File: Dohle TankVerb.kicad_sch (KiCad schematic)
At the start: 10 parts, among them J1 AudioJack3, J2 AudioJack3, J3 PWR, J4 Conn_01x07_Female, SW1 3pdt_footswitch, SW2 SW_Push

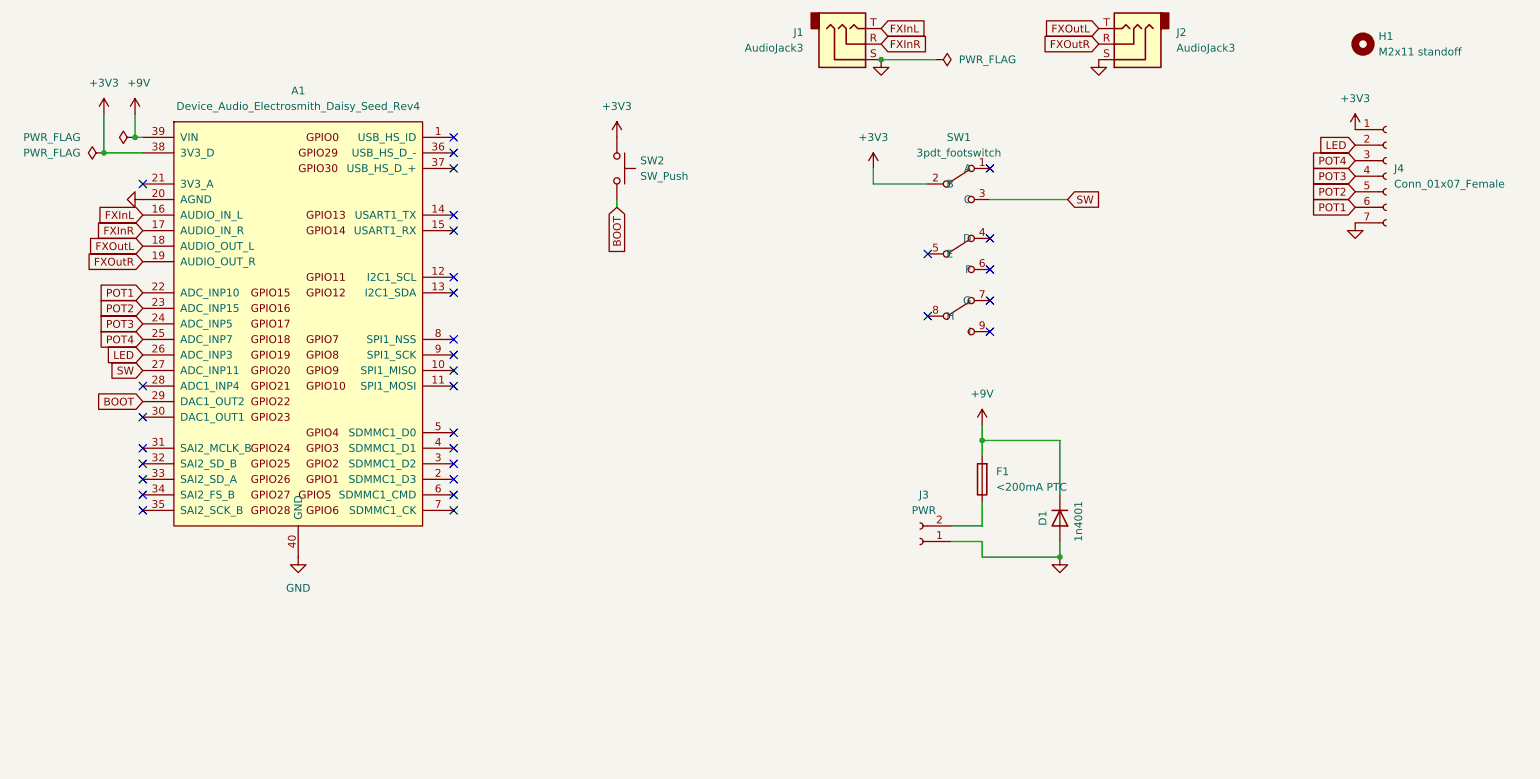
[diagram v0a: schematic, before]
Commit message: Finish adding the expression pedal. New release.
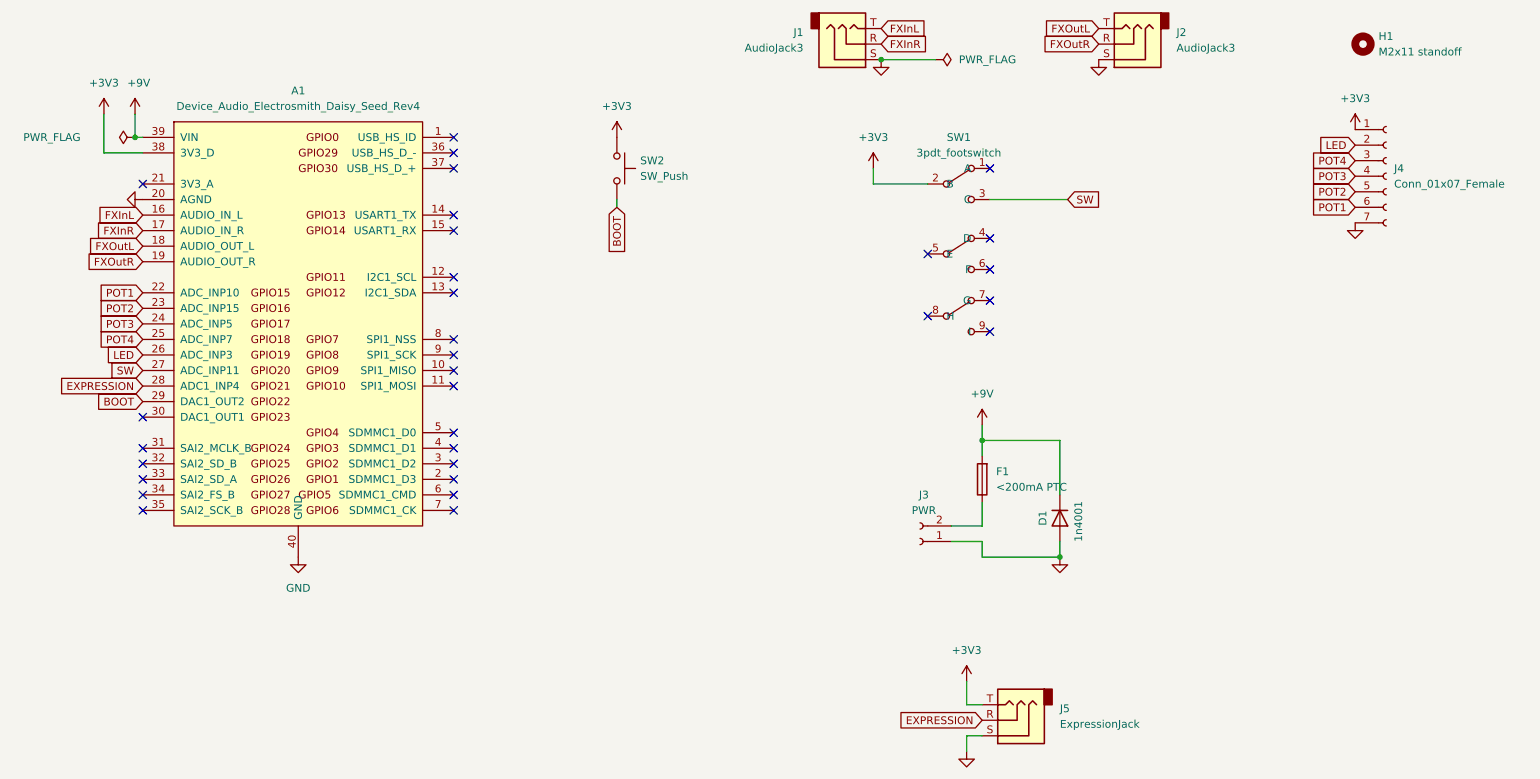
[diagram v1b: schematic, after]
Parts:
- added J5: ExpressionJack, BirdFootprints:ExpressionJack, symbol Connector:AudioJack3
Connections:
- net +3V3: now also J5.T
- net GND: now also J5.S
- net EXPRESSION: now reaches A1.28 (ADC1_INP4)
- net EXPRESSION: now also J5.R
- no-connect marks 32 -> 31
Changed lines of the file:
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@@
   (junction (at 39.37 48.26) (diameter 0) (color 0 0 0 0)
-  )
-  (junction (at 34.29 50.8) (diameter 0) (color 0 0 0 0)
   )
   (junction (at 190.5 116.84) (diameter 0) (color 0 0 0 0)
@@
   (no_connect (at 40.64 106.68))
   (no_connect (at 40.64 109.22))
-  (no_connect (at 40.64 88.9))
   (no_connect (at 91.44 109.22))
   (no_connect (at 91.44 106.68))
@@
     (stroke (width 0) (type default) (color 0 0 0 0))
   )
+  (wire (pts (xy 177.8 146.05) (xy 175.26 146.05))
+    (stroke (width 0) (type default) (color 0 0 0 0))
+  )
   (wire (pts (xy 40.64 50.8) (xy 34.29 50.8))
     (stroke (width 0) (type default) (color 0 0 0 0))
   )
+  (wire (pts (xy 175.26 140.97) (xy 177.8 140.97))
+    (stroke (width 0) (type default) (color 0 0 0 0))
+  )
+  (wire (pts (xy 175.26 146.05) (xy 175.26 148.59))
+    (stroke (width 0) (type default) (color 0 0 0 0))
+  )
   (wire (pts (xy 161.29 35.56) (xy 170.18 35.56))
     (stroke (width 0) (type default) (color 0 0 0 0))
   )
   (wire (pts (xy 177.8 111.76) (xy 177.8 107.95))
+    (stroke (width 0) (type default) (color 0 0 0 0))
+  )
+  (wire (pts (xy 175.26 137.16) (xy 175.26 140.97))
     (stroke (width 0) (type default) (color 0 0 0 0))
   )
@@
     )
   )
+  (global_label "EXPRESSION" (shape input) (at 177.8 143.51 180) (fields_autoplaced)
+    (effects (font (size 1.27 1.27)) (justify right))
+    (property "Intersheet References" "${INTERSHEET_REFS}" (id 0) (at 163.6545 143.4306 0)
+      (effects (font (size 1.27 1.27)) (justify right) hide)
+    )
+  )
   (global_label "FXInR" (shape input) (at 161.29 33.02 0) (fields_autoplaced)
     (effects (font (size 1.27 1.27)) (justify left))
@@
     (effects (font (size 1.27 1.27)) (justify right))
     (property "Intersheet References" "${INTERSHEET_REFS}" (id 0) (at 231.5693 57.2294 0)
+      (effects (font (size 1.27 1.27)) (justify right) hide)
+    )
+  )
+  (global_label "EXPRESSION" (shape input) (at 40.64 88.9 180) (fields_autoplaced)
+    (effects (font (size 1.27 1.27)) (justify right))
+    (property "Intersheet References" "${INTERSHEET_REFS}" (id 0) (at 26.4945 88.8206 0)
       (effects (font (size 1.27 1.27)) (justify right) hide)
     )
@@
     (pin "9")
   )
+  (symbol (lib_id "power:GND") (at 175.26 148.59 0) (unit 1)
+    (in_bom yes) (on_board yes) (fields_autoplaced)
+    (property "Reference" "#PWR02" (id 0) (at 175.26 154.94 0)
+      (effects (font (size 1.27 1.27)) hide)
+    )
+    (property "Value" "GND" (id 1) (at 175.26 153.035 0)
+      (effects (font (size 1.27 1.27)) hide)
+    )
+    (property "Footprint" "" (id 2) (at 175.26 148.59 0)
+      (effects (font (size 1.27 1.27)) hide)
+    )
+    (property "Datasheet" "" (id 3) (at 175.26 148.59 0)
+      (effects (font (size 1.27 1.27)) hide)
+    )
+    (pin "1")
+  )
   (symbol (lib_id "power:PWR_FLAG") (at 39.37 48.26 90) (unit 1)
     (in_bom yes) (on_board yes)
@@
     (pin "T")
   )
+  (symbol (lib_id "Connector:AudioJack3") (at 182.88 143.51 180) (unit 1)
+    (in_bom yes) (on_board yes) (fields_autoplaced)
+    (property "Reference" "J5" (id 0) (at 190.5 141.6049 0)
+      (effects (font (size 1.27 1.27)) (justify right))
+    )
+    (property "Value" "ExpressionJack" (id 1) (at 190.5 144.1449 0)
+      (effects (font (size 1.27 1.27)) (justify right))
+    )
+    (property "Footprint" "BirdFootprints:ExpressionJack" (id 2) (at 182.88 143.51 0)
+      (effects (font (size 1.27 1.27)) hide)
+    )
+    (property "Datasheet" "~" (id 3) (at 182.88 143.51 0)
+      (effects (font (size 1.27 1.27)) hide)
+    )
+    (pin "R")
+    (pin "S")
+    (pin "T")
+  )
   (symbol (lib_id "power:GND") (at 238.76 62.23 0) (unit 1)
     (in_bom yes) (on_board yes) (fields_autoplaced)
@@
     )
     (property "Datasheet" "" (id 3) (at 34.29 44.45 0)
-      (effects (font (size 1.27 1.27)) hide)
-    )
-    (pin "1")
-  )
-  (symbol (lib_id "power:PWR_FLAG") (at 34.29 50.8 90) (unit 1)
-    (in_bom yes) (on_board yes) (fields_autoplaced)
-    (property "Reference" "#FLG0101" (id 0) (at 32.385 50.8 0)
-      (effects (font (size 1.27 1.27)) hide)
-    )
-    (property "Value" "PWR_FLAG" (id 1) (at 30.48 50.7999 90)
-      (effects (font (size 1.27 1.27)) (justify left))
-    )
-    (property "Footprint" "" (id 2) (at 34.29 50.8 0)
-      (effects (font (size 1.27 1.27)) hide)
-    )
-    (property "Datasheet" "~" (id 3) (at 34.29 50.8 0)
       (effects (font (size 1.27 1.27)) hide)
     )
@@
     (pin "9")
   )
+  (symbol (lib_id "power:+3V3") (at 175.26 137.16 0) (unit 1)
+    (in_bom yes) (on_board yes) (fields_autoplaced)
+    (property "Reference" "#PWR01" (id 0) (at 175.26 140.97 0)
+      (effects (font (size 1.27 1.27)) hide)
+    )
+    (property "Value" "+3V3" (id 1) (at 175.26 132.08 0))
+    (property "Footprint" "" (id 2) (at 175.26 137.16 0)
+      (effects (font (size 1.27 1.27)) hide)
+    )
+    (property "Datasheet" "" (id 3) (at 175.26 137.16 0)
+      (effects (font (size 1.27 1.27)) hide)
+    )
+    (pin "1")
+  )
   (symbol (lib_id "Connector:Conn_01x02_Female") (at 167.64 114.3 180) (unit 1)
     (in_bom yes) (on_board yes) (fields_autoplaced)
@@
   )
   (symbol_instances
-    (path "/5d3b1520-4846-48a2-8f8d-69acf5d56f23"
-      (reference "#FLG0101") (unit 1) (value "PWR_FLAG") (footprint "")
-    )
     (path "/2f1e17a0-da25-4944-8c9c-ca9b735e70f8"
       (reference "#FLG0102") (unit 1) (value "PWR_FLAG") (footprint "")
@@
       (reference "#FLG0103") (unit 1) (value "PWR_FLAG") (footprint "")
     )
+    (path "/971569c7-0bc7-4978-abb2-1c167e784d8d"
+      (reference "#PWR01") (unit 1) (value "+3V3") (footprint "")
+    )
+    (path "/1eef872a-2b4b-494e-9965-bfd7b728cba9"
+      (reference "#PWR02") (unit 1) (value "GND") (footprint "")
+    )
     (path "/5a207532-5461-4b4f-a011-cd6fb0198e5c"
       (reference "#PWR0101") (unit 1) (value "+3V3") (footprint "")
@@
       (reference "J4") (unit 1) (value "Conn_01x07_Female") (footprint "Connector_PinSocket_2.54mm:PinSocket_1x07_P2.54mm_Vertical")
     )
+    (path "/49ca1d29-0ee4-4489-926b-7a376fb3a7ef"
+      (reference "J5") (unit 1) (value "ExpressionJack") (footprint "BirdFootprints:ExpressionJack")
+    )
     (path "/111c38f7-ec2b-444f-8ec0-61814dc6a219"
